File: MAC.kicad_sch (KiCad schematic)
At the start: 23 parts, among them J10 Conn_01x30_Male, SW1 RotaryEncoder_Switch, U12 LM358_DFN

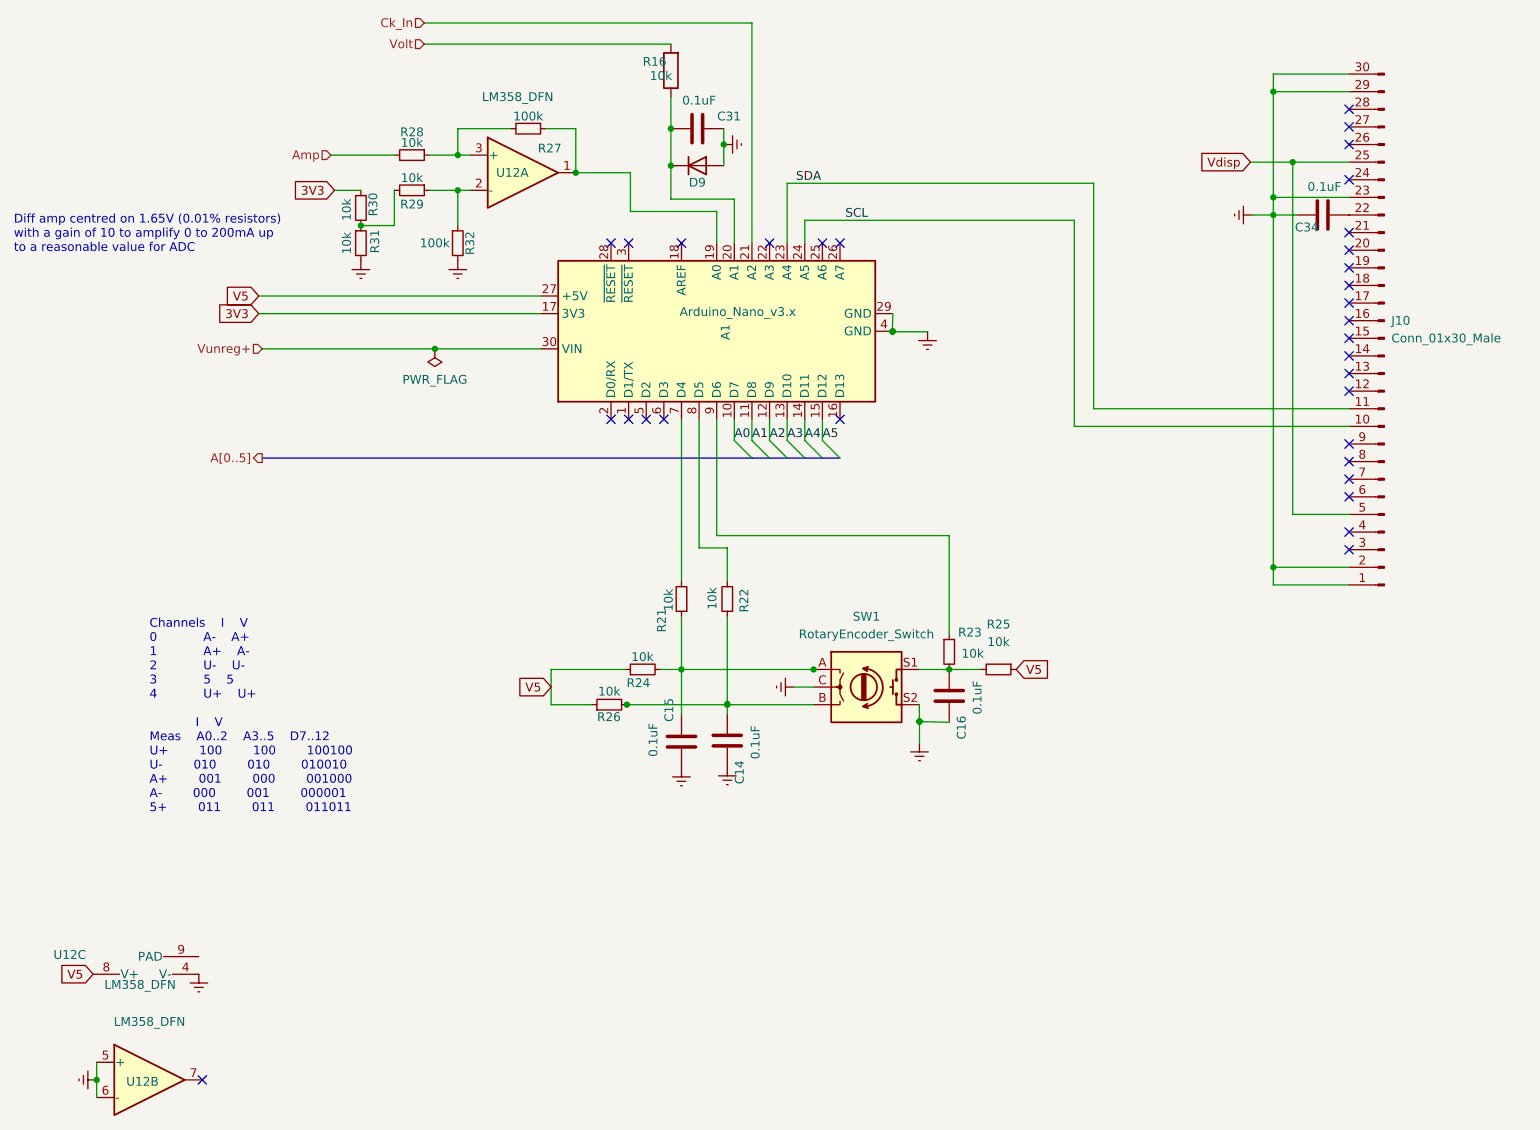
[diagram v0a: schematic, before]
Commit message: added new op amps and used automated traces due to complexity
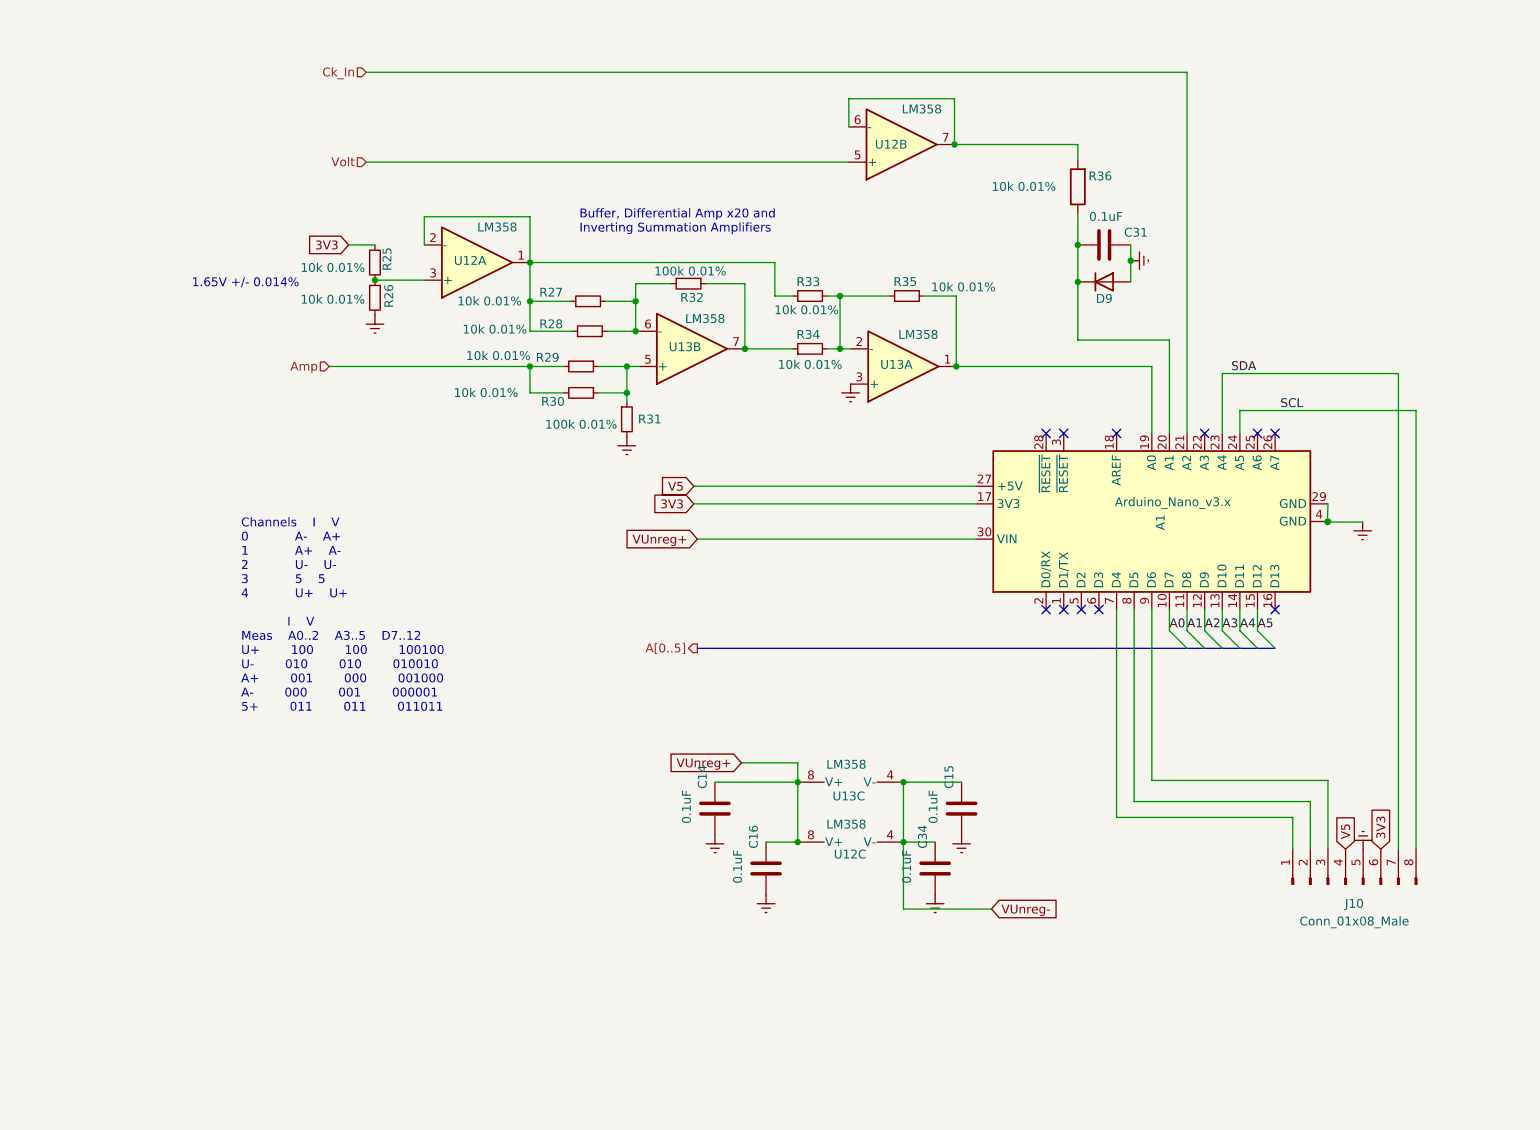
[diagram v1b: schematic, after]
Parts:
- removed J10: Conn_01x30_Male, WE SMD Side 30 Pin:687130149022, symbol Connector:Conn_01x30_Male
- removed R21, R22, R23, R24, R25, R26: 10k, Resistor_SMD:R_0603_1608Metric, symbol Device:R_Small
- removed SW1: RotaryEncoder_Switch, Rotary_Encoder:RotaryEncoder_Alps_EC11E-Switch_Vertical_H20mm_CircularMountingHoles, symbol Device:RotaryEncoder_Switch
- added J10: Conn_01x08_Male, Connector_PinHeader_2.54mm:PinHeader_1x08_P2.54mm_Vertical, symbol Connector:Conn_01x08_Male
- added R27, R30, R33, R34, R35: 10k 0.01%, Resistor_SMD:R_0603_1608Metric, symbol Device:R_Small
- added U13: LM358, Package_SO:TSSOP-8_4.4x3mm_P0.65mm, symbol Amplifier_Operational:LM358
- R25: renamed from R30; value 10k -> 10k 0.01%
- R26: renamed from R31; value 10k -> 10k 0.01%
- R28, R29: value 10k -> 10k 0.01%
- R31: renamed from R32; value 100k -> 100k 0.01%
- R32: renamed from R27; value 100k -> 100k 0.01%
- R36: renamed from R16; value 10k -> 10k 0.01%
- U12: value LM358_DFN -> LM358; footprint Package_DFN_QFN:DFN-8-1EP_2x2mm_P0.5mm_EP1.05x1.75mm -> Package_SO:TSSOP-8_4.4x3mm_P0.65mm; symbol Amplifier_Operational:LM358_DFN -> Amplifier_Operational:LM358
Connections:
- net 3V3: now also J10.6 (Pin_6)
- net Amp: now also R29.2, R30.2; no longer R28.2
- net GNDREF: now also C14.2, C16.2, J10.5 (Pin_5), U13.3 (+); no longer C14.1, C16.1, U12.4 (V-), U12.5 (+), U12.6 (-)
- net SCL: now also J10.8 (Pin_8)
- net SDA: now also J10.7 (Pin_7)
- net V5: now also J10.4 (Pin_4); no longer U12.8 (V+)
- net Volt: now also U12.5 (+); no longer R36.2
- net at A1.9 (D6): now also J10.3 (Pin_3)
- net VUnreg-: now reaches C15.1
- net VUnreg-: now also C34.1, U12.4 (V-), U13.4 (V-)
- net at A1.8 (D5): now also J10.2 (Pin_2)
- net at R29.1, R31.1: now also R30.1, U13.5 (+); no longer U12.2 (-)
- net at R25.2, R26.1: now also U12.3 (+); no longer R29.2
- net at A1.7 (D4): now also J10.1 (Pin_1)
- net Vunreg+ renamed VUnreg+
- net VUnreg+: now also C14.1, C16.1, U12.8 (V+), U13.8 (V+)
- new net: R36.2, U12.6 (-), U12.7
- new net: R27.1, R28.1, R33.1, U12.1, U12.2 (-)
- new net: R27.2, R28.2, R32.2, U13.6 (-)
- new net: A1.19 (A0), R35.2, U13.1
- new net: R33.2, R34.2, R35.1, U13.2 (-)
- new net: R32.1, R34.1, U13.7
- no-connect marks 32 -> 11
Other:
- note added: "1.65V +/- 0.014%"
- note added: "Buffer, Differential Amp x20 and Inverting Summation Amplifiers"
- note removed: "Diff amp centred on 1.65V (0.01% resistors) with a gain of 10 to amplify 0 to 200mA up to a reasonable value for ADC"
- moved on the sheet: A1, C31, D9, R25, R26, R29, R31, R32, R36, U12A, U12B

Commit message: new EMC-EMI layout with improved suppression
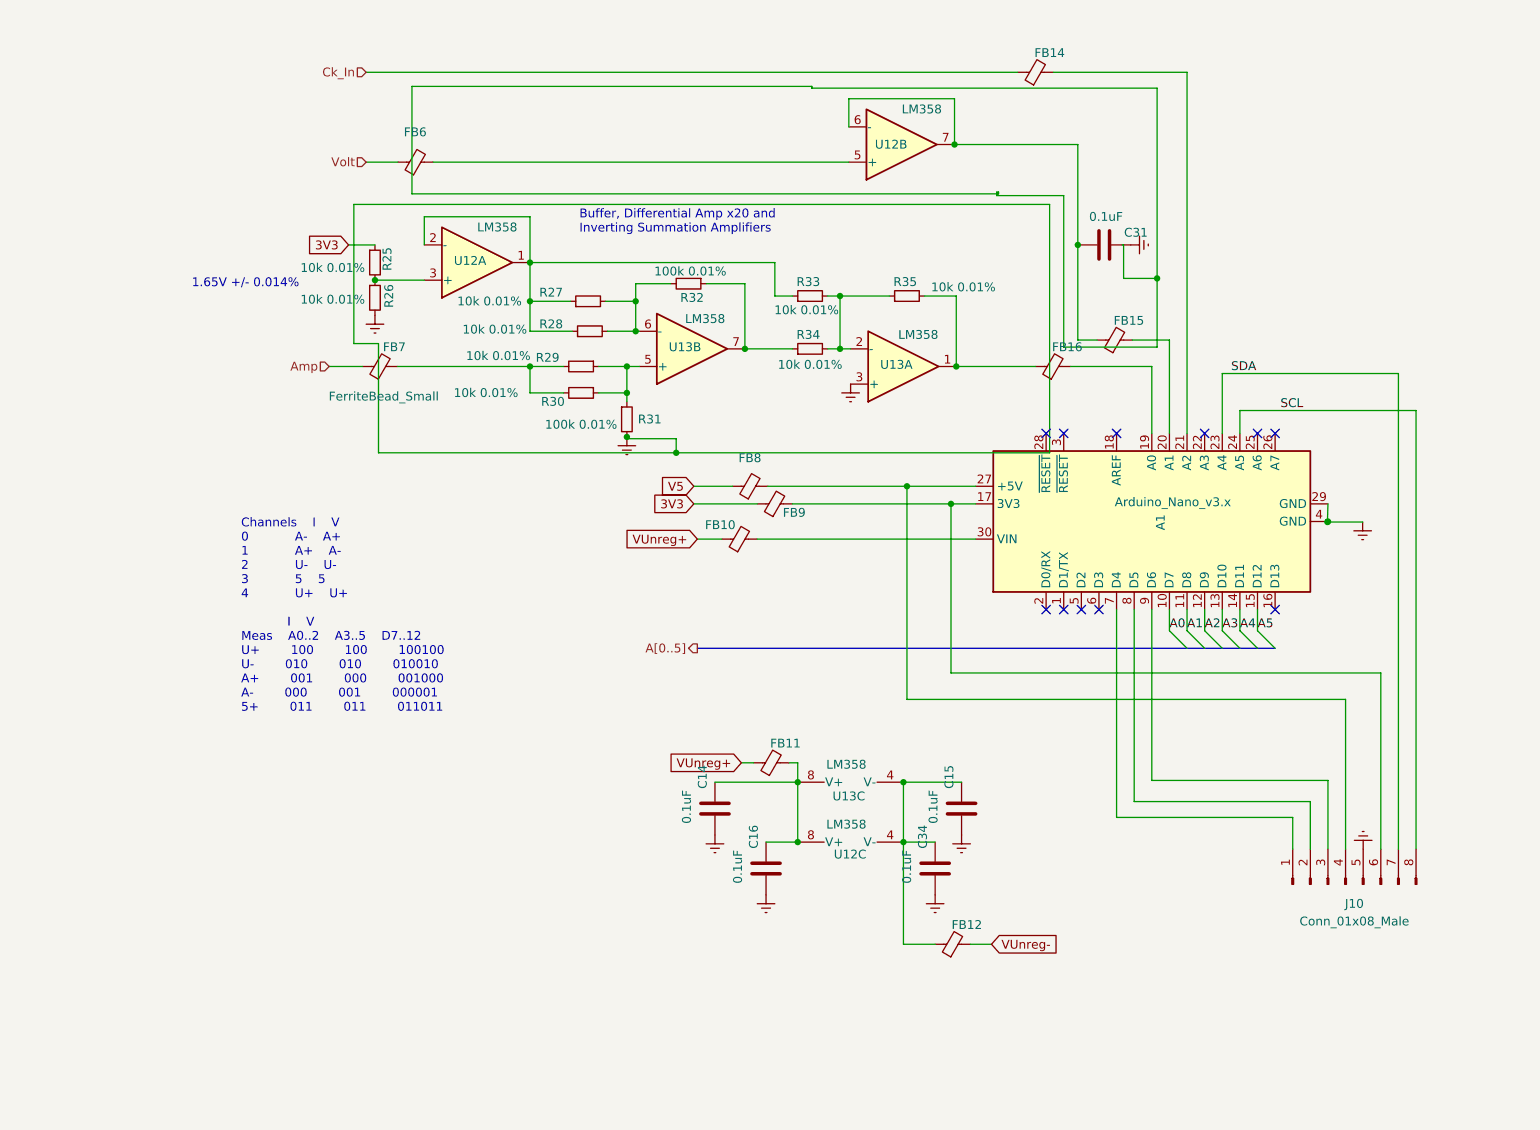
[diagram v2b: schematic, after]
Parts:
- removed D9: S1K-13-F, Diode_SMD:D_SMA, symbol Simulation_SPICE:DIODE
- removed R36: 10k 0.01%, Resistor_SMD:R_0603_1608Metric, symbol Device:R
- added FB10, FB11, FB12, FB14, FB15, FB16, FB6, FB7, FB8, FB9: FerriteBead_Small, Inductor_SMD:L_0603_1608Metric, symbol Device:FerriteBead_Small
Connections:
- net 3V3: now also FB9.1; no longer A1.17 (3V3), J10.6 (Pin_6)
- net Amp: now also FB7.1; no longer R29.2, R30.2
- net Ck_In: now also FB14.1; no longer A1.21 (A2)
- net V5: now also FB8.1; no longer A1.27 (+5V), J10.4 (Pin_4)
- net VUnreg+: now also FB10.1, FB11.1; no longer A1.30 (VIN), C14.1, C16.1, U12.8 (V+), U13.8 (V+)
- net VUnreg-: now also FB12.2; no longer C15.1, C34.1, U12.4 (V-), U13.4 (V-)
- net Volt: now also FB6.1; no longer U12.5 (+)
- net at C31.2: now also U12.6 (-), U12.7, FB15.1; no longer A1.20 (A1)
- net at R35.2, U13.1: now also FB16.1; no longer A1.19 (A0)
- new net: C14.1, C16.1, FB11.2, U12.8 (V+), U13.8 (V+)
- new net: C15.1, C34.1, FB12.1, U12.4 (V-), U13.4 (V-)
- new net: FB7.2, R29.2, R30.2
- new net: A1.17 (3V3), FB9.2, J10.6 (Pin_6)
- new net: A1.27 (+5V), FB8.2, J10.4 (Pin_4)
- new net: FB6.2, U12.5 (+)
- new net: A1.21 (A2), FB14.2
- new net: A1.19 (A0), FB16.2
- new net: A1.20 (A1), FB15.2
- new net: A1.30 (VIN), FB10.2

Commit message: updates with foot print guard rings
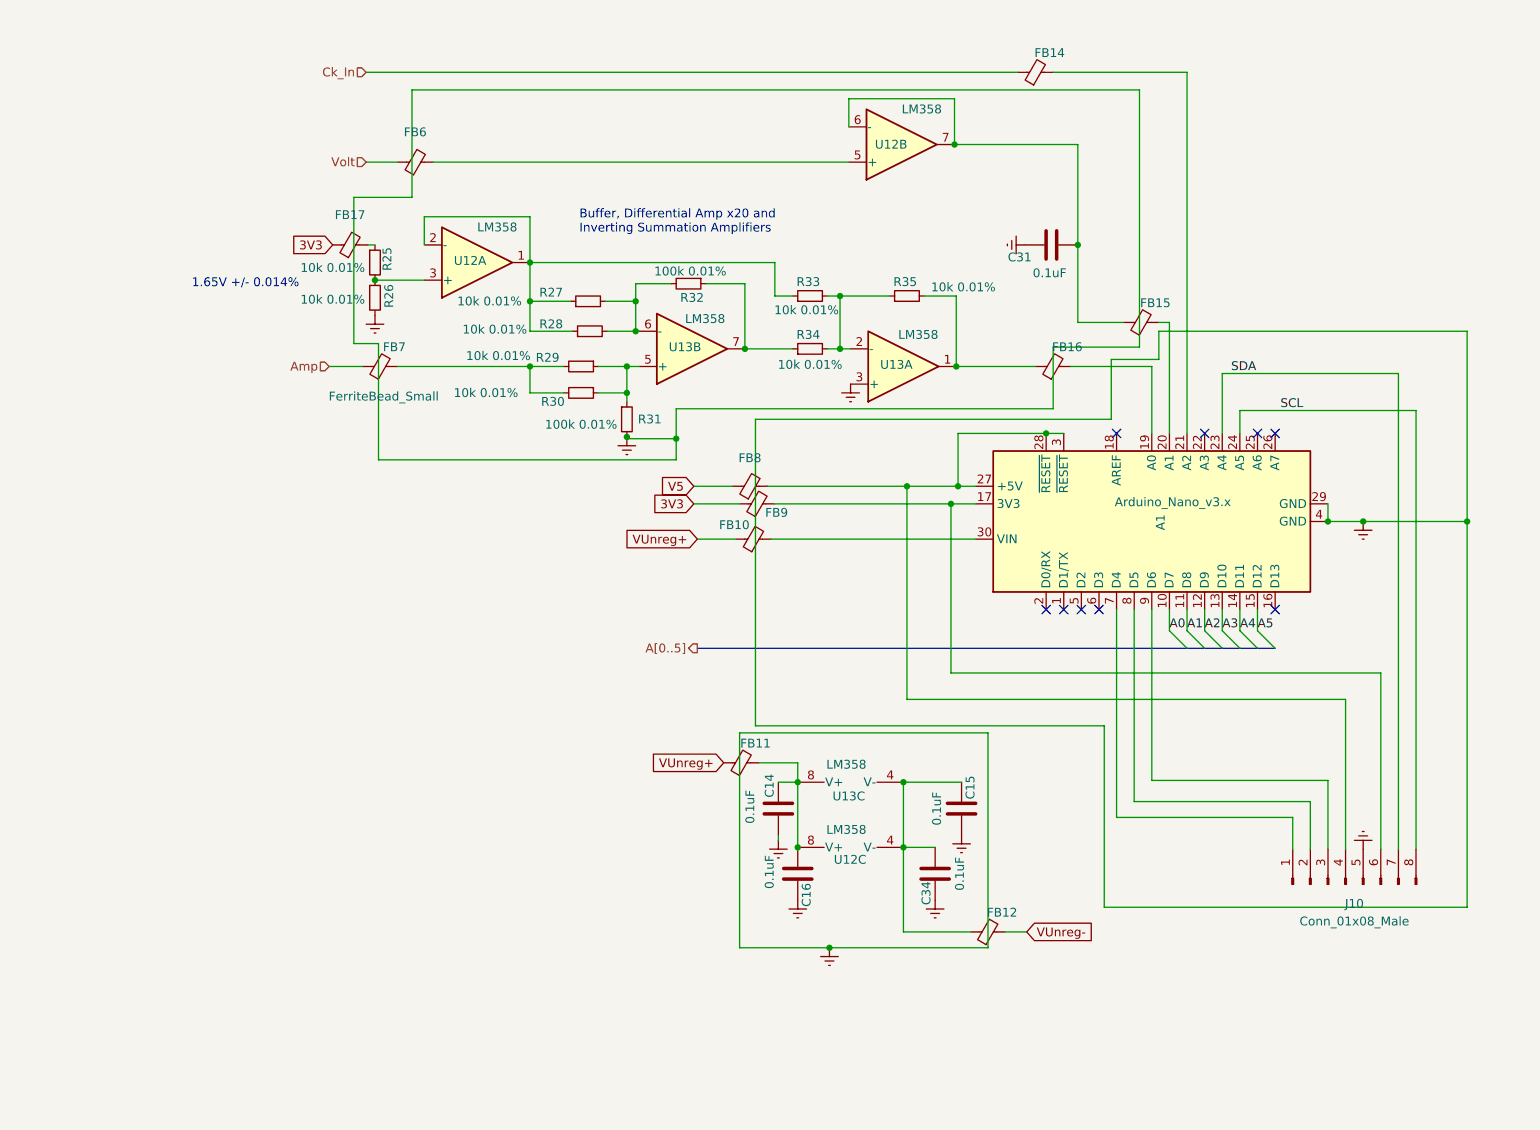
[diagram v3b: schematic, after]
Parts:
- added FB17: FerriteBead_Small, Inductor_SMD:L_0603_1608Metric, symbol Device:FerriteBead_Small
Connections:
- net 3V3: now also FB17.1; no longer R25.1
- net at A1.27 (+5V), FB8.2, J10.4 (Pin_4): now also A1.28 (~{RESET}), A1.3 (~{RESET})
- new net: FB17.2, R25.1
- no-connect marks 11 -> 9
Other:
- note removed: "Channels I V 0 A- A+ 1 A+ A- 2 U- U- 3 5 5 4 U+ U+ I V Meas A0..2 A3..5 D7..12 U+ 100 100 100100 U- 010 010 010010 A+ 001 000 001000 A- 000 001 000001 5+ 011 011 011011"
- moved on the sheet: C14, C16, C31, C34, FB10, FB11, FB12, FB15, FB9, U12C

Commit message: working on MUX and pre-amp layout
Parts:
- added C37: 0.1uF, Capacitor_SMD:C_0603_1608Metric, symbol Device:C
- renumbered U13 to U12, U12 to U13
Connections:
- net GNDREF: now also C37.2
- net at J10.1 (Pin_1): now also A1.5 (D2); no longer A1.7 (D4)
- net at J10.2 (Pin_2): now also A1.6 (D3); no longer A1.8 (D5)
- net at J10.3 (Pin_3): now also A1.7 (D4); no longer A1.9 (D6)
- net at R25.2, R26.1, U12.3 (+): now also C37.1
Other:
- note added: "1.65V ± 0.014%"
- note removed: "1.65V +/- 0.014%"
- moved on the sheet: C14, C15, C16, C34, FB11, FB12, R29, R30, U12C, U13C
